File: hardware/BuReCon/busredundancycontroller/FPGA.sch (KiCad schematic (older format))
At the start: 1 part, among them U1 ICE40LP1K-CM36

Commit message: House Keeping
House keeping
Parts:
- U1: footprint UCBGA36_LAT -> ICE40LP1K-CM36:ICE40LP1K-CM36
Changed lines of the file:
@@
 F 0 "U1" H 6050 2887 60  0000 C CNN
 F 1 "ICE40LP1K-CM36" H 6050 2781 60  0000 C CNN
-F 2 "UCBGA36_LAT" H 6050 2740 60  0001 C CNN
+F 2 "ICE40LP1K-CM36:ICE40LP1K-CM36" H 6050 2740 60  0001 C CNN
 F 3 "" H 4550 2400 60  0000 C CNN
 	1    4550 2400

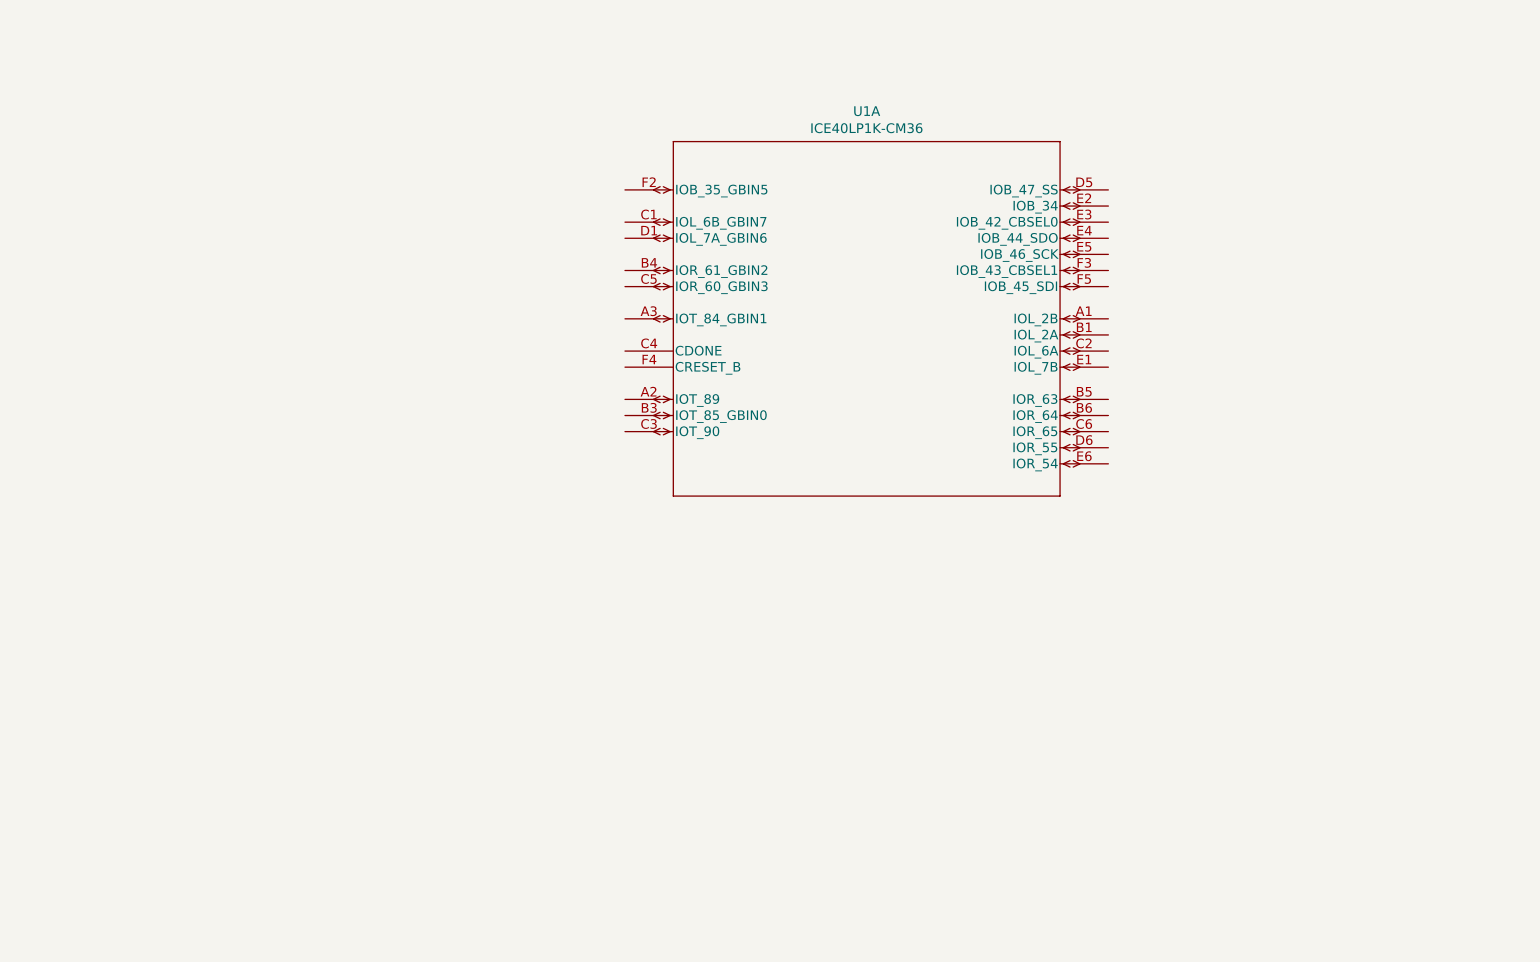
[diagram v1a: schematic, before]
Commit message: FPGA configuration
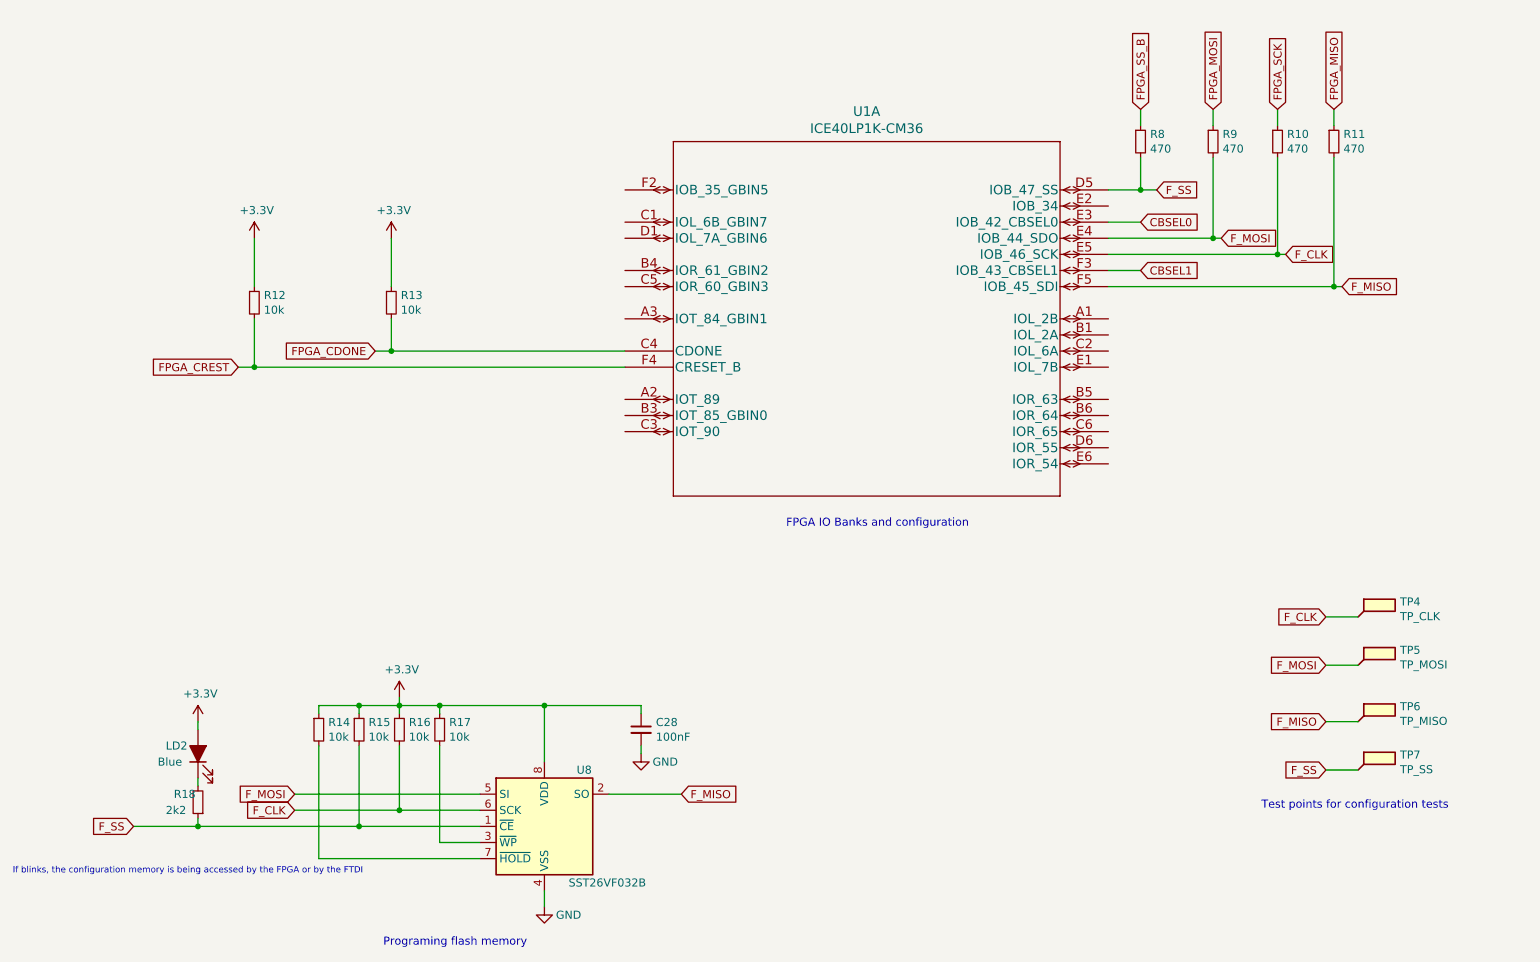
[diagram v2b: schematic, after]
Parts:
- added C28: 100nF, symbol Device:C_Small
- added LD2: Blue, LED_SMD:LED_0201_0603Metric, symbol Device:LED_ALT
- added R10, R11, R8, R9: 470, symbol Device:R_Small
- added R12, R13, R14, R15, R16, R17: 10k, symbol Device:R_Small
- added R18: 2k2, symbol Device:R_Small
- added TP4: TP_CLK, TestPoint:TestPoint_Plated_Hole_D3.0mm, symbol Connector:TestPoint_Flag
- added TP5: TP_MOSI, TestPoint:TestPoint_Plated_Hole_D3.0mm, symbol Connector:TestPoint_Flag
- added TP6: TP_MISO, TestPoint:TestPoint_Plated_Hole_D3.0mm, symbol Connector:TestPoint_Flag
- added TP7: TP_SS, TestPoint:TestPoint_Plated_Hole_D3.0mm, symbol Connector:TestPoint_Flag
- added U8: SST26VF032B, Package_SO:SOIC-8_5.275x5.275mm_P1.27mm, symbol Memory_Flash:SST25VF080B-50-4x-S2Ax
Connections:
- net FPGA_CDONE: now reaches U1.C4 (CDONE)
- net FPGA_CDONE: now also R13.2
- net F_SS: now reaches U1.D5 (IOB_47_SS)
- net F_SS: now also R15.2, R18.1, R8.2, TP7.1, U8.1 (~CE)
- net CBSEL0: now reaches U1.E3 (IOB_42_CBSEL0)
- net F_MOSI: now reaches U1.E4 (IOB_44_SDO)
- net F_MOSI: now also R9.2, TP5.1, U8.5 (SI)
- net F_CLK: now reaches U1.E5 (IOB_46_SCK)
- net F_CLK: now also R10.2, R16.2, TP4.1, U8.6 (SCK)
- net CBSEL1: now reaches U1.F3 (IOB_43_CBSEL1)
- net FPGA_CREST: now reaches U1.F4 (CRESET_B)
- net FPGA_CREST: now also R12.2
- net F_MISO: now reaches U1.F5 (IOB_45_SDI)
- net F_MISO: now also R11.2, TP6.1, U8.2 (SO)
- new net: R17.2, U8.3 (~WP~)
- new net: R14.2, U8.7 (~HOLD~)
- new net: LD2.1 (K), R18.2
- new net +3V3: C28.1, LD2.2 (A), R12.1, R13.1, R14.1, R15.1, R16.1, R17.1, U8.8 (VDD)
- new net FPGA_MISO: R11.1
- new net FPGA_MOSI: R9.1
- new net FPGA_SCK: R10.1
- new net FPGA_SS_B: R8.1
- new net GND: C28.2, U8.4 (VSS)
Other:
- note added: "FPGA IO Banks and configuration"
- note added: "If blinks, the configuration memory is being accessed by the FPGA or by the FTDI"
- note added: "Programing flash memory"
- note added: "Test points for configuration tests"

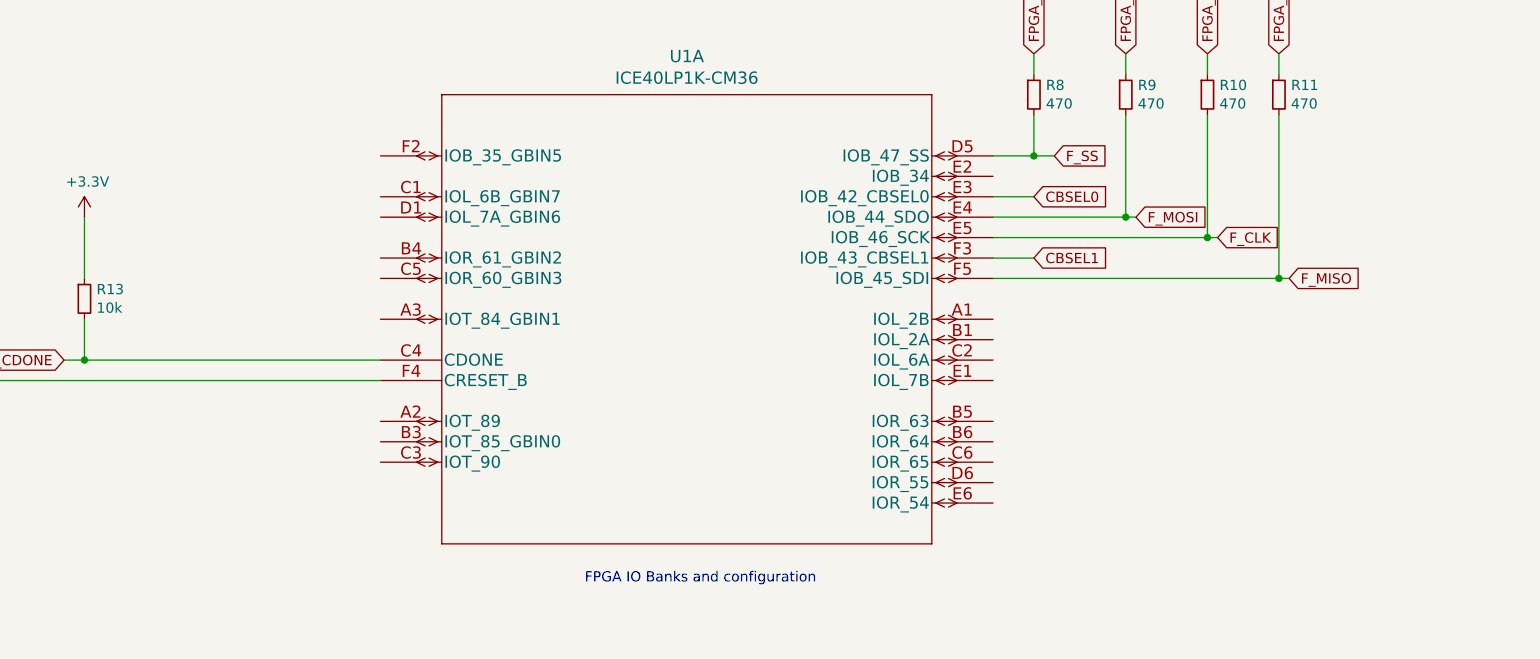
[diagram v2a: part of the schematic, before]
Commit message: Cleanup and IO banks
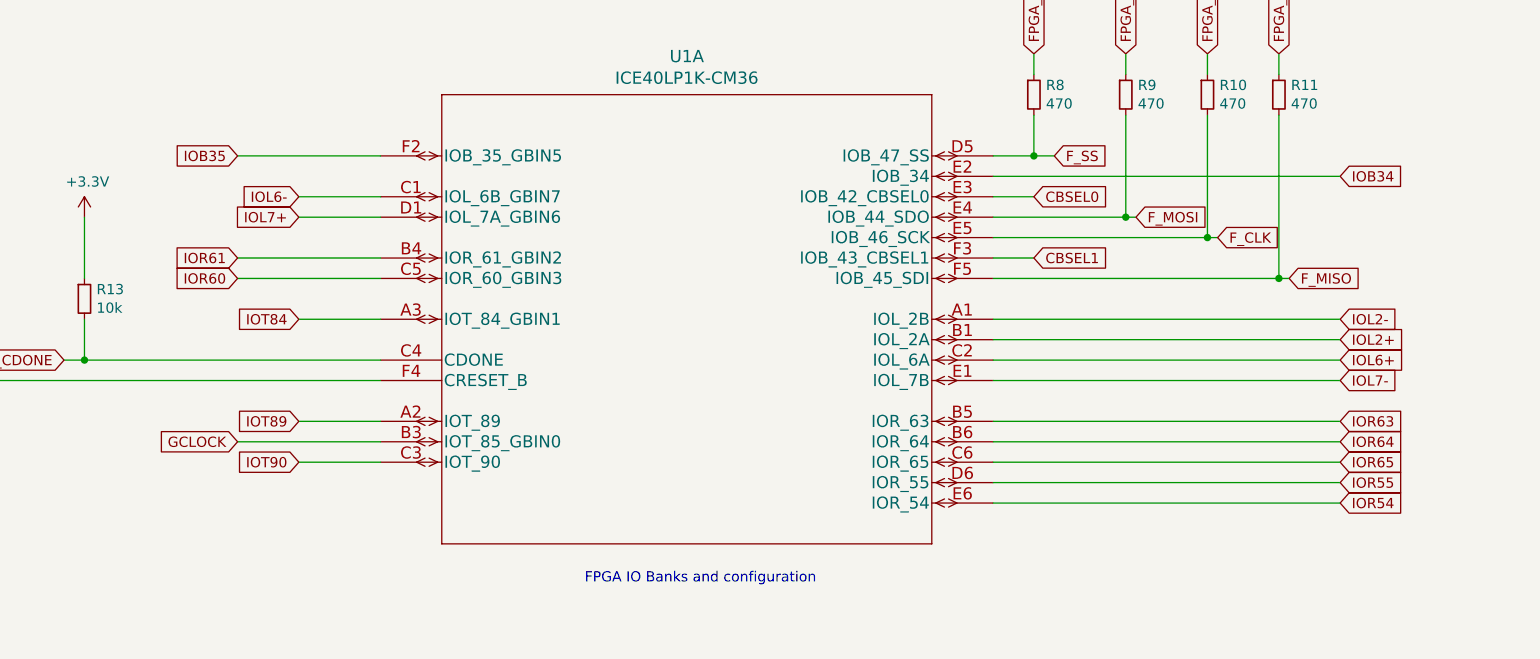
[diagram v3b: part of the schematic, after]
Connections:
- net IOL2-: now reaches U1.A1 (IOL_2B)
- net IOT89: now reaches U1.A2 (IOT_89)
- net IOT84: now reaches U1.A3 (IOT_84_GBIN1)
- net IOL2+: now reaches U1.B1 (IOL_2A)
- net GCLOCK: now reaches U1.B3 (IOT_85_GBIN0)
- net IOR61: now reaches U1.B4 (IOR_61_GBIN2)
- net IOR63: now reaches U1.B5 (IOR_63)
- net IOR64: now reaches U1.B6 (IOR_64)
- net IOL6-: now reaches U1.C1 (IOL_6B_GBIN7)
- net IOL6+: now reaches U1.C2 (IOL_6A)
- net IOT90: now reaches U1.C3 (IOT_90)
- net IOR60: now reaches U1.C5 (IOR_60_GBIN3)
- net IOR65: now reaches U1.C6 (IOR_65)
- net IOL7+: now reaches U1.D1 (IOL_7A_GBIN6)
- net IOR55: now reaches U1.D6 (IOR_55)
- net IOL7-: now reaches U1.E1 (IOL_7B)
- net IOB34: now reaches U1.E2 (IOB_34)
- net IOR54: now reaches U1.E6 (IOR_54)
- net IOB35: now reaches U1.F2 (IOB_35_GBIN5)
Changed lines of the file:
@@
 Text Notes 750  6650 0    39   ~ 0
 If blinks, the configuration memory is being accessed by the FPGA or by the FTDI
+Text GLabel 3850 3800 0    50   Input ~ 0
+GCLOCK
+Text GLabel 9250 2500 2    50   Input ~ 0
+IOB34
+Wire Wire Line
+	7550 2500 9250 2500
+Text GLabel 9250 3700 2    50   Input ~ 0
+IOR63
+Text GLabel 9250 3800 2    50   Input ~ 0
+IOR64
+Text GLabel 9250 3900 2    50   Input ~ 0
+IOR65
+Text GLabel 9250 4000 2    50   Input ~ 0
+IOR55
+Text GLabel 9250 4100 2    50   Input ~ 0
+IOR54
+Wire Wire Line
+	7550 3700 9250 3700
+Wire Wire Line
+	7550 3800 9250 3800
+Wire Wire Line
+	7550 3900 9250 3900
+Wire Wire Line
+	7550 4000 9250 4000
+Wire Wire Line
+	7550 4100 9250 4100
+Text GLabel 9250 3300 2    50   Input ~ 0
+IOL2+
+Text GLabel 9250 3200 2    50   Input ~ 0
+IOL2-
+Wire Wire Line
+	9250 3200 7550 3200
+Wire Wire Line
+	9250 3300 7550 3300
+Text GLabel 9250 3400 2    50   Input ~ 0
+IOL6+
+Text GLabel 4150 2600 0    50   Input ~ 0
+IOL6-
+Wire Wire Line
+	4150 2600 4550 2600
+Wire Wire Line
+	9250 3400 7550 3400
+Text GLabel 9250 3500 2    50   Input ~ 0
+IOL7-
+Wire Wire Line
+	9250 3500 7550 3500
+Text GLabel 4150 2700 0    50   Input ~ 0
+IOL7+
+Wire Wire Line
+	4150 2700 4550 2700
+Text GLabel 3850 2900 0    50   Input ~ 0
+IOR61
+Wire Wire Line
+	3850 2900 4550 2900
+Text GLabel 3850 3000 0    50   Input ~ 0
+IOR60
+Wire Wire Line
+	3850 3000 4550 3000
+Text GLabel 3850 2400 0    50   Input ~ 0
+IOB35
+Wire Wire Line
+	3850 2400 4550 2400
+Text GLabel 4150 3200 0    50   Input ~ 0
+IOT84
+Wire Wire Line
+	4150 3200 4550 3200
+Text GLabel 4150 3700 0    50   Input ~ 0
+IOT89
+Wire Wire Line
+	3850 3800 4550 3800
+Wire Wire Line
+	4150 3700 4550 3700
+Text GLabel 4150 3900 0    50   Input ~ 0
+IOT90
+Wire Wire Line
+	4150 3900 4550 3900
 $EndSCHEMATC

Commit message: Connectors and RS232
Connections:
- net IOB34 renamed FT_TXD
- net IOR65 renamed FT_RXD
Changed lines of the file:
@@
 Text GLabel 3850 3800 0    50   Input ~ 0
 GCLOCK
-Text GLabel 9250 2500 2    50   Input ~ 0
-IOB34
 Wire Wire Line
 	7550 2500 9250 2500
@@
 Text GLabel 9250 3800 2    50   Input ~ 0
 IOR64
-Text GLabel 9250 3900 2    50   Input ~ 0
-IOR65
 Text GLabel 9250 4000 2    50   Input ~ 0
 IOR55
@@
 Wire Wire Line
 	7550 3800 9250 3800
-Wire Wire Line
-	7550 3900 9250 3900
 Wire Wire Line
 	7550 4000 9250 4000
@@
 Wire Wire Line
 	4150 3900 4550 3900
+Text GLabel 9650 3900 2    50   Input ~ 0
+FT_RXD
+Wire Wire Line
+	7550 3900 9650 3900
+Text GLabel 9250 2500 2    50   Input ~ 0
+FT_TXD
 $EndSCHEMATC

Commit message: Footprints, Initial PCB
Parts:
- C28: footprint (none) -> Capacitor_SMD:C_0603_1608Metric
- LD2: footprint LED_SMD:LED_0201_0603Metric -> LED_SMD:LED_0603_1608Metric
- R10, R11, R12, R13, R14, R15, R16, R17, R18, R8, R9: footprint (none) -> Resistor_SMD:R_0603_1608Metric
- TP4, TP5, TP6, TP7: footprint TestPoint:TestPoint_Plated_Hole_D3.0mm -> TestPoint:TestPoint_Pad_D1.0mm
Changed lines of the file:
@@
 F 0 "R12" H 2309 3146 50  0000 L CNN
 F 1 "10k" H 2309 3055 50  0000 L CNN
-F 2 "" H 2250 3100 50  0001 C CNN
+F 2 "Resistor_SMD:R_0603_1608Metric" H 2250 3100 50  0001 C CNN
 F 3 "~" H 2250 3100 50  0001 C CNN
 	1    2250 3100
@@
 F 0 "R13" H 3159 3146 50  0000 L CNN
 F 1 "10k" H 3159 3055 50  0000 L CNN
-F 2 "" H 3100 3100 50  0001 C CNN
+F 2 "Resistor_SMD:R_0603_1608Metric" H 3100 3100 50  0001 C CNN
 F 3 "~" H 3100 3100 50  0001 C CNN
 	1    3100 3100
@@
 F 0 "R8" H 7809 2146 50  0000 L CNN
 F 1 "470" H 7809 2055 50  0000 L CNN
-F 2 "" H 7750 2100 50  0001 C CNN
+F 2 "Resistor_SMD:R_0603_1608Metric" H 7750 2100 50  0001 C CNN
 F 3 "~" H 7750 2100 50  0001 C CNN
 	1    7750 2100
@@
 F 0 "R9" H 8259 2146 50  0000 L CNN
 F 1 "470" H 8259 2055 50  0000 L CNN
-F 2 "" H 8200 2100 50  0001 C CNN
+F 2 "Resistor_SMD:R_0603_1608Metric" H 8200 2100 50  0001 C CNN
 F 3 "~" H 8200 2100 50  0001 C CNN
 	1    8200 2100
@@
 F 0 "R10" H 8659 2146 50  0000 L CNN
 F 1 "470" H 8659 2055 50  0000 L CNN
-F 2 "" H 8600 2100 50  0001 C CNN
+F 2 "Resistor_SMD:R_0603_1608Metric" H 8600 2100 50  0001 C CNN
 F 3 "~" H 8600 2100 50  0001 C CNN
 	1    8600 2100
@@
 F 0 "R11" H 9009 2146 50  0000 L CNN
 F 1 "470" H 9009 2055 50  0000 L CNN
-F 2 "" H 8950 2100 50  0001 C CNN
+F 2 "Resistor_SMD:R_0603_1608Metric" H 8950 2100 50  0001 C CNN
 F 3 "~" H 8950 2100 50  0001 C CNN
 	1    8950 2100
@@
 F 0 "R18" H 2050 6150 50  0000 R CNN
 F 1 "2k2" H 2100 6250 50  0000 R CNN
-F 2 "" H 1900 6200 50  0001 C CNN
+F 2 "Resistor_SMD:R_0603_1608Metric" H 1900 6200 50  0001 C CNN
 F 3 "~" H 1900 6200 50  0001 C CNN
 	1    1900 6200
@@
 F 0 "LD2" V 1950 6100 50  0000 R CNN
 F 1 "Blue" V 1850 6150 50  0000 R CNN
-F 2 "LED_SMD:LED_0201_0603Metric" H 1900 5900 50  0001 C CNN
+F 2 "LED_SMD:LED_0603_1608Metric" H 1900 5900 50  0001 C CNN
 F 3 "~" H 1900 5900 50  0001 C CNN
 	1    1900 5900
@@
 F 0 "R17" H 3459 5796 50  0000 L CNN
 F 1 "10k" H 3459 5705 50  0000 L CNN
-F 2 "" H 3400 5750 50  0001 C CNN
+F 2 "Resistor_SMD:R_0603_1608Metric" H 3400 5750 50  0001 C CNN
 F 3 "~" H 3400 5750 50  0001 C CNN
 	1    3400 5750
@@
 F 0 "R16" H 3209 5796 50  0000 L CNN
 F 1 "10k" H 3209 5705 50  0000 L CNN
-F 2 "" H 3150 5750 50  0001 C CNN
+F 2 "Resistor_SMD:R_0603_1608Metric" H 3150 5750 50  0001 C CNN
 F 3 "~" H 3150 5750 50  0001 C CNN
 	1    3150 5750
@@
 F 0 "R15" H 2959 5796 50  0000 L CNN
 F 1 "10k" H 2959 5705 50  0000 L CNN
-F 2 "" H 2900 5750 50  0001 C CNN
+F 2 "Resistor_SMD:R_0603_1608Metric" H 2900 5750 50  0001 C CNN
 F 3 "~" H 2900 5750 50  0001 C CNN
 	1    2900 5750
@@
 F 0 "R14" H 2709 5796 50  0000 L CNN
 F 1 "10k" H 2709 5705 50  0000 L CNN
-F 2 "" H 2650 5750 50  0001 C CNN
+F 2 "Resistor_SMD:R_0603_1608Metric" H 2650 5750 50  0001 C CNN
 F 3 "~" H 2650 5750 50  0001 C CNN
 	1    2650 5750
@@
 F 0 "C28" H 4742 5796 50  0000 L CNN
 F 1 "100nF" H 4742 5705 50  0000 L CNN
-F 2 "" H 4650 5750 50  0001 C CNN
+F 2 "Capacitor_SMD:C_0603_1608Metric" H 4650 5750 50  0001 C CNN
 F 3 "~" H 4650 5750 50  0001 C CNN
 	1    4650 5750
@@
 F 0 "TP4" H 9360 5144 50  0000 L CNN
 F 1 "TP_CLK" H 9360 5053 50  0000 L CNN
-F 2 "TestPoint:TestPoint_Plated_Hole_D3.0mm" H 9300 5050 50  0001 C CNN
+F 2 "TestPoint:TestPoint_Pad_D1.0mm" H 9300 5050 50  0001 C CNN
 F 3 "~" H 9300 5050 50  0001 C CNN
 	1    9100 5050
@@
 F 0 "TP5" H 9360 5444 50  0000 L CNN
 F 1 "TP_MOSI" H 9360 5353 50  0000 L CNN
-F 2 "TestPoint:TestPoint_Plated_Hole_D3.0mm" H 9300 5350 50  0001 C CNN
+F 2 "TestPoint:TestPoint_Pad_D1.0mm" H 9300 5350 50  0001 C CNN
 F 3 "~" H 9300 5350 50  0001 C CNN
 	1    9100 5350
@@
 F 0 "TP6" H 9360 5794 50  0000 L CNN
 F 1 "TP_MISO" H 9360 5703 50  0000 L CNN
-F 2 "TestPoint:TestPoint_Plated_Hole_D3.0mm" H 9300 5700 50  0001 C CNN
+F 2 "TestPoint:TestPoint_Pad_D1.0mm" H 9300 5700 50  0001 C CNN
 F 3 "~" H 9300 5700 50  0001 C CNN
 	1    9100 5700
@@
 F 0 "TP7" H 9360 6094 50  0000 L CNN
 F 1 "TP_SS" H 9360 6003 50  0000 L CNN
-F 2 "TestPoint:TestPoint_Plated_Hole_D3.0mm" H 9300 6000 50  0001 C CNN
+F 2 "TestPoint:TestPoint_Pad_D1.0mm" H 9300 6000 50  0001 C CNN
 F 3 "~" H 9300 6000 50  0001 C CNN
 	1    9100 6000
